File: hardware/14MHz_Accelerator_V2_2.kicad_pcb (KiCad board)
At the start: 2 copper layers, 84 x 89 mm, 42 parts, among them J1 68K_Host_Interface, J2 TEST_POINT, J3 CDAC IN, U1 512K*8_SRAM, U10 74ACT32, U11 TLC555CD, U2 MC68HC000, U3 512K*8_SRAM, U4 74ACT02, U5 74HCT74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

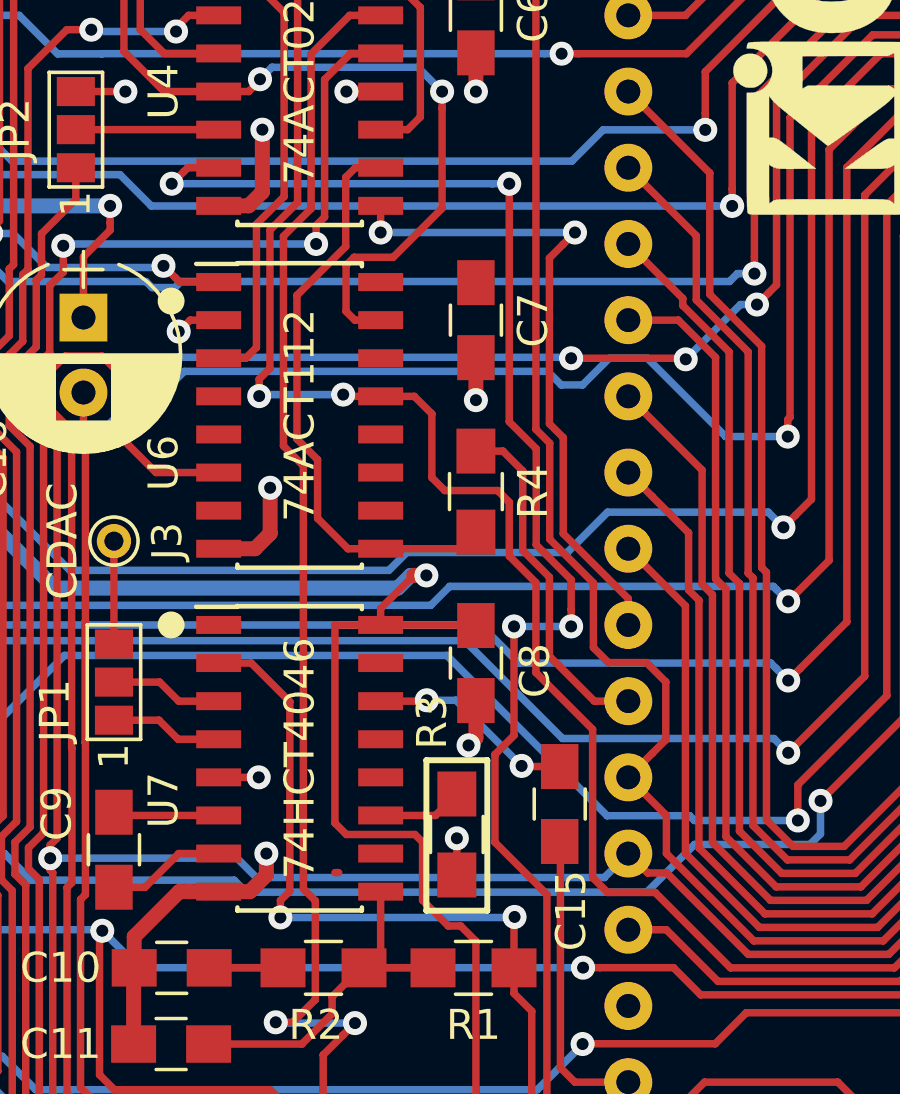
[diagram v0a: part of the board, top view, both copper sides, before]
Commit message: minor layout optimizations
added bill of materials
added pictures
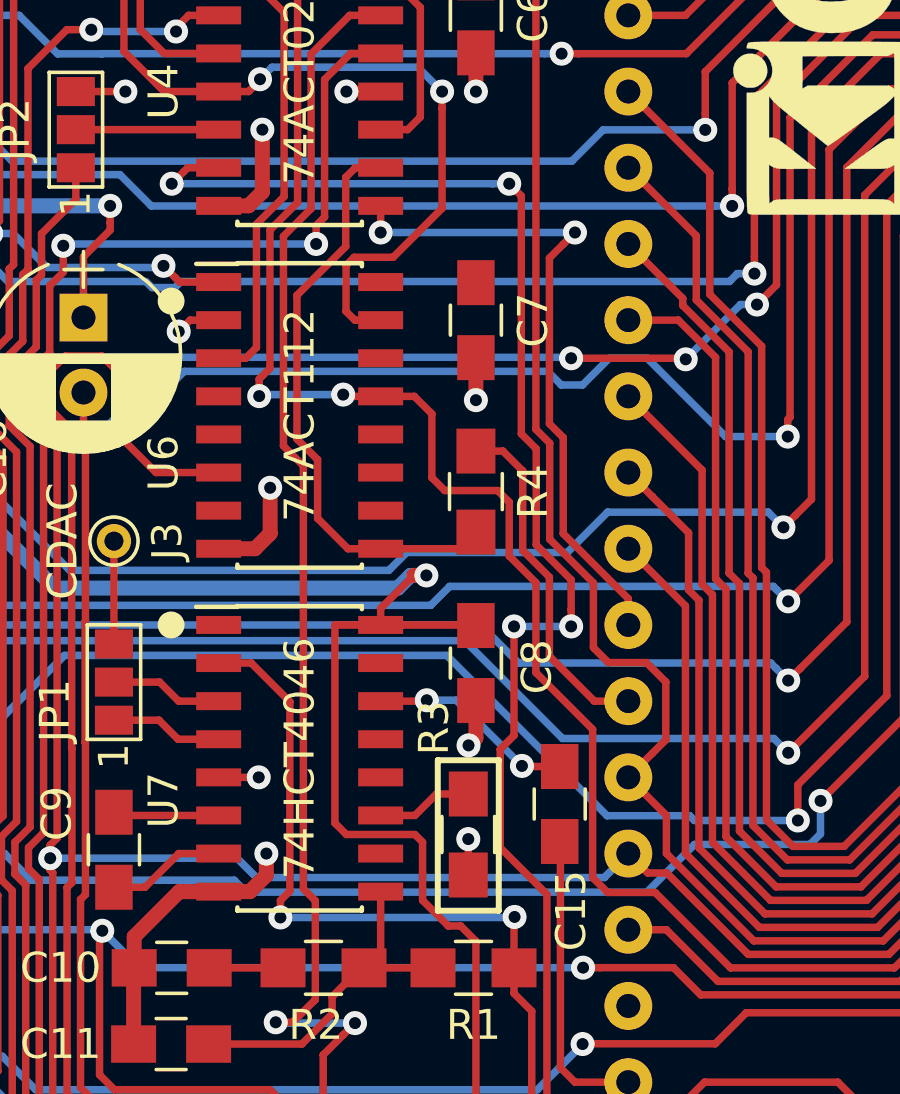
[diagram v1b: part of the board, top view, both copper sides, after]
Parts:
- moved R3 0.38 mm to (91.2, 93.3)
